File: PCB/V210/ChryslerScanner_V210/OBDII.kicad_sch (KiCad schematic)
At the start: 3 parts

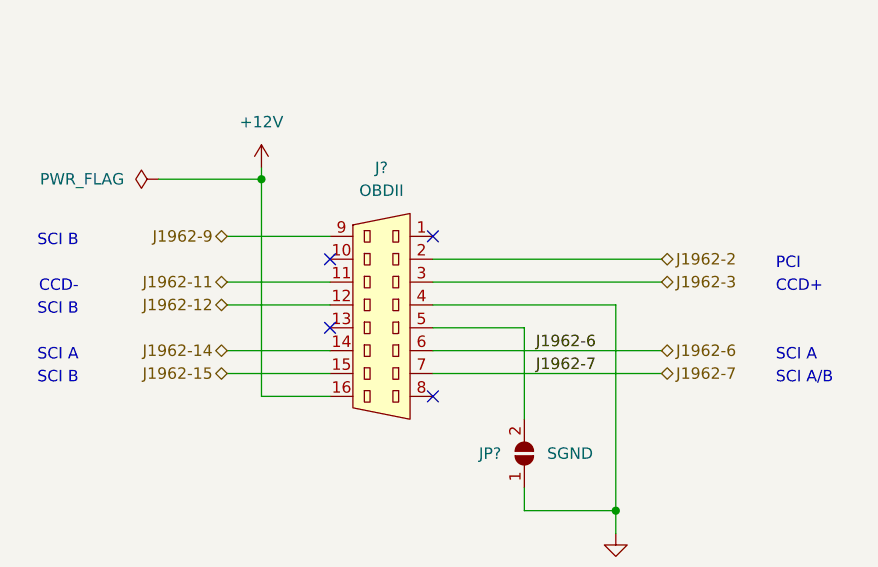
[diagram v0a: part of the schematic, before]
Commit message: Added power supplies. Removed CCD.
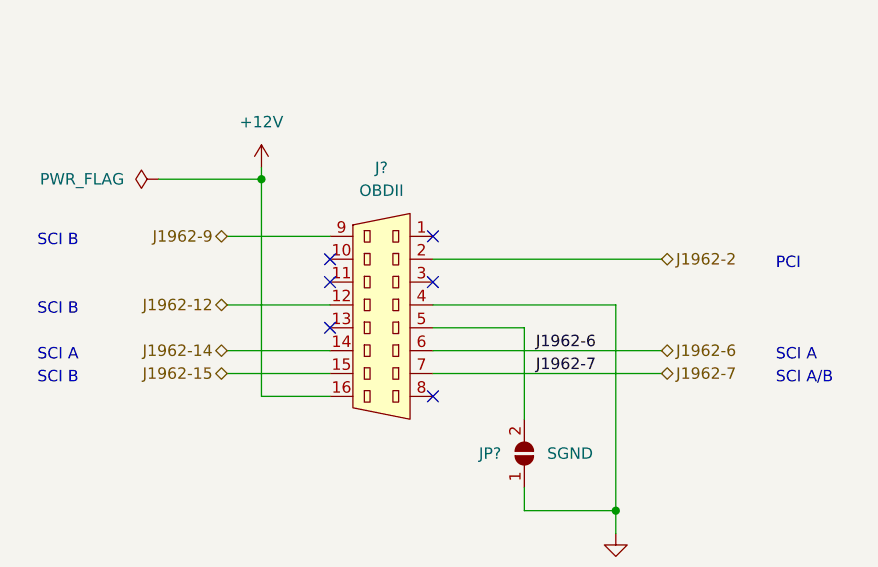
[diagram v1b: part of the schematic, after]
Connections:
- net J1962-11: no longer names the net of J?.11
- net J1962-3: no longer names the net of J?.3
- no-connect marks 4 -> 6
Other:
- note removed: "CCD+"
- note removed: "CCD-"
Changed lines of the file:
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@@
   (title_block
     (title "Chrysler Scanner")
-    (date "2023-06-24")
+    (date "2023-06-25")
     (rev "V2.11")
     (company "andy@britishideas.com")
@@
   (no_connect (at 151.13 92.71))
   (no_connect (at 151.13 110.49))
+  (no_connect (at 151.13 97.79))
+  (no_connect (at 139.7 97.79))
   (wire (pts (xy 151.13 95.25) (xy 176.53 95.25))
     (stroke (width 0) (type default) (color 0 0 0 0))
   )
   (wire (pts (xy 128.27 92.71) (xy 139.7 92.71))
-    (stroke (width 0) (type default) (color 0 0 0 0))
-  )
-  (wire (pts (xy 151.13 97.79) (xy 176.53 97.79))
     (stroke (width 0) (type default) (color 0 0 0 0))
   )
@@
   )
   (wire (pts (xy 128.27 105.41) (xy 139.7 105.41))
-    (stroke (width 0) (type default) (color 0 0 0 0))
-  )
-  (wire (pts (xy 128.27 97.79) (xy 139.7 97.79))
     (stroke (width 0) (type default) (color 0 0 0 0))
   )
@@
     (effects (font (size 1.27 1.27)) (justify left bottom))
   )
-  (text "CCD-" (at 111.76 99.06 180)
-    (effects (font (size 1.27 1.27)) (justify right bottom))
-  )
   (text "PCI" (at 189.23 96.52 0)
     (effects (font (size 1.27 1.27)) (justify left bottom))
@@
   (text "SCI B" (at 111.76 109.22 180)
     (effects (font (size 1.27 1.27)) (justify right bottom))
-  )
-  (text "CCD+" (at 189.23 99.06 0)
-    (effects (font (size 1.27 1.27)) (justify left bottom))
   )
   (text "SCI A" (at 189.23 106.68 0)
@@
     (effects (font (size 1.27 1.27)) (justify left))
   )
-  (hierarchical_label "J1962-3" (shape bidirectional) (at 176.53 97.79 0)
-    (effects (font (size 1.27 1.27)) (justify left))
-  )
-  (hierarchical_label "J1962-11" (shape bidirectional) (at 128.27 97.79 180)
-    (effects (font (size 1.27 1.27)) (justify right))
-  )
   (hierarchical_label "J1962-12" (shape bidirectional) (at 128.27 100.33 180)

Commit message: Completed schematic.
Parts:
- gave numbers to parts that had none: 3
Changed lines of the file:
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@@
   (symbol (lib_id "Connector_Generic:Conn_01x02") (at 135.89 60.96 0) (mirror y) (unit 1)
     (in_bom yes) (on_board yes) (fields_autoplaced)
-    (property "Reference" "J?" (id 0) (at 135.89 54.61 0))
+    (property "Reference" "J3" (id 0) (at 135.89 54.61 0))
     (property "Value" "SCI" (id 1) (at 135.89 57.15 0))
     (property "Footprint" "" (id 2) (at 135.89 60.96 0)
@@
   (symbol (lib_id "Jumper:SolderJumper_2_Open") (at 161.29 116.84 90) (unit 1)
     (in_bom yes) (on_board yes)
-    (property "Reference" "JP?" (id 0) (at 157.48 116.84 90))
+    (property "Reference" "JP1" (id 0) (at 157.48 116.84 90))
     (property "Value" "SGND" (id 1) (at 166.37 116.84 90))
     (property "Footprint" "" (id 2) (at 161.29 116.84 0)
@@
   (symbol (lib_id "power:PWR_FLAG") (at 120.65 86.36 90) (unit 1)
     (in_bom yes) (on_board yes) (fields_autoplaced)
-    (property "Reference" "#FLG?" (id 0) (at 118.745 86.36 0)
+    (property "Reference" "#FLG02" (id 0) (at 118.745 86.36 0)
       (effects (font (size 1.27 1.27)) hide)
     )
@@
   (symbol (lib_id "power:GND") (at 171.45 125.73 0) (unit 1)
     (in_bom yes) (on_board yes) (fields_autoplaced)
-    (property "Reference" "#PWR?" (id 0) (at 171.45 132.08 0)
+    (property "Reference" "#PWR042" (id 0) (at 171.45 132.08 0)
       (effects (font (size 1.27 1.27)) hide)
     )
@@
   (symbol (lib_id "power:+12V") (at 132.08 85.09 0) (unit 1)
     (in_bom yes) (on_board yes) (fields_autoplaced)
-    (property "Reference" "#PWR?" (id 0) (at 132.08 88.9 0)
+    (property "Reference" "#PWR041" (id 0) (at 132.08 88.9 0)
       (effects (font (size 1.27 1.27)) hide)
     )
@@
   (symbol (lib_id "ChryslerScanner:OBDII") (at 143.51 105.41 0) (unit 1)
     (in_bom yes) (on_board yes) (fields_autoplaced)
-    (property "Reference" "J?" (id 0) (at 145.415 85.09 0))
+    (property "Reference" "J4" (id 0) (at 145.415 85.09 0))
     (property "Value" "OBDII" (id 1) (at 145.415 87.63 0))
     (property "Footprint" "" (id 2) (at 143.51 105.41 0)

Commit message: WIP
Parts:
- removed J3: SCI, symbol Connector_Generic:Conn_01x02
- added J2: PCI, Britishideas:PhoenixContact_COMBICON_PT_3, symbol Connector:Screw_Terminal_01x03
- JP1: footprint (none) -> Jumper:SolderJumper-2_P1.3mm_Open_TrianglePad1.0x1.5mm
- renumbered J4 to J3
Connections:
- net +12V: now also J2.1 (Pin_1)
- net GND: now also J2.3 (Pin_3)
- net J1962-2: now also J2.2 (Pin_2)
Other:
- title: Chrysler Scanner -> TJ Diag
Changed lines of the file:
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@@
   (paper "A4")
   (title_block
-    (title "Chrysler Scanner")
-    (date "2023-06-25")
-    (rev "V2.11")
+    (title "TJ Diag")
+    (date "2023-07-01")
+    (rev "V1.00")
     (company "andy@britishideas.com")
     (comment 1 "V210/ChryslerScanner_V210/schematic/ChryslerScanner_V210_schematic.pdf")
@@
     (stroke (width 0) (type default) (color 0 0 0 0))
   )
+  (wire (pts (xy 143.51 59.69) (xy 140.97 59.69))
+    (stroke (width 0) (type default) (color 0 0 0 0))
+  )
   (wire (pts (xy 128.27 92.71) (xy 139.7 92.71))
     (stroke (width 0) (type default) (color 0 0 0 0))
@@
     (stroke (width 0) (type default) (color 0 0 0 0))
   )
-  (wire (pts (xy 140.97 60.96) (xy 149.86 60.96))
+  (wire (pts (xy 140.97 57.15) (xy 149.86 57.15))
     (stroke (width 0) (type default) (color 0 0 0 0))
   )
@@
     (stroke (width 0) (type default) (color 0 0 0 0))
   )
+  (wire (pts (xy 143.51 62.23) (xy 143.51 59.69))
+    (stroke (width 0) (type default) (color 0 0 0 0))
+  )
   (wire (pts (xy 151.13 107.95) (xy 176.53 107.95))
     (stroke (width 0) (type default) (color 0 0 0 0))
   )
-  (wire (pts (xy 140.97 63.5) (xy 149.86 63.5))
+  (wire (pts (xy 143.51 54.61) (xy 140.97 54.61))
     (stroke (width 0) (type default) (color 0 0 0 0))
   )
@@
   )
   (wire (pts (xy 151.13 105.41) (xy 176.53 105.41))
+    (stroke (width 0) (type default) (color 0 0 0 0))
+  )
+  (wire (pts (xy 143.51 52.07) (xy 143.51 54.61))
     (stroke (width 0) (type default) (color 0 0 0 0))
   )
@@
     (effects (font (size 1.27 1.27)) (justify left bottom))
   )
-  (label "J1962-7" (at 162.56 107.95 0)
-    (effects (font (size 1.27 1.27)) (justify left bottom))
-  )
-  (label "J1962-7" (at 149.86 63.5 0)
-    (effects (font (size 1.27 1.27)) (justify left bottom))
-  )
-  (label "J1962-6" (at 149.86 60.96 0)
-    (effects (font (size 1.27 1.27)) (justify left bottom))
-  )
-  (label "J1962-6" (at 162.56 105.41 0)
+  (label "J1962-2" (at 162.56 95.25 0)
+    (effects (font (size 1.27 1.27)) (justify left bottom))
+  )
+  (label "J1962-2" (at 149.86 57.15 0)
     (effects (font (size 1.27 1.27)) (justify left bottom))
   )
@@
     (effects (font (size 1.27 1.27)) (justify right))
   )
-  (symbol (lib_id "Connector_Generic:Conn_01x02") (at 135.89 60.96 0) (mirror y) (unit 1)
-    (in_bom yes) (on_board yes) (fields_autoplaced)
-    (property "Reference" "J3" (id 0) (at 135.89 54.61 0))
-    (property "Value" "SCI" (id 1) (at 135.89 57.15 0))
-    (property "Footprint" "" (id 2) (at 135.89 60.96 0)
-      (effects (font (size 1.27 1.27)) hide)
-    )
-    (property "Datasheet" "~" (id 3) (at 135.89 60.96 0)
+  (symbol (lib_id "Connector:Screw_Terminal_01x03") (at 135.89 57.15 0) (mirror y) (unit 1)
+    (in_bom yes) (on_board yes) (fields_autoplaced)
+    (property "Reference" "J2" (id 0) (at 135.89 48.26 0))
+    (property "Value" "PCI" (id 1) (at 135.89 50.8 0))
+    (property "Footprint" "Britishideas:PhoenixContact_COMBICON_PT_3" (id 2) (at 135.89 57.15 0)
+      (effects (font (size 1.27 1.27)) hide)
+    )
+    (property "Datasheet" "~" (id 3) (at 135.89 57.15 0)
+      (effects (font (size 1.27 1.27)) hide)
+    )
+    (property "manf#" "1935174" (id 4) (at 135.89 57.15 0)
       (effects (font (size 1.27 1.27)) hide)
     )
     (pin "1")
     (pin "2")
+    (pin "3")
   )
   (symbol (lib_id "Jumper:SolderJumper_2_Open") (at 161.29 116.84 90) (unit 1)
@@
     (property "Reference" "JP1" (id 0) (at 157.48 116.84 90))
     (property "Value" "SGND" (id 1) (at 166.37 116.84 90))
-    (property "Footprint" "" (id 2) (at 161.29 116.84 0)
+    (property "Footprint" "Jumper:SolderJumper-2_P1.3mm_Open_TrianglePad1.0x1.5mm" (id 2) (at 161.29 116.84 0)
       (effects (font (size 1.27 1.27)) hide)
     )
@@
   (symbol (lib_id "power:GND") (at 171.45 125.73 0) (unit 1)
     (in_bom yes) (on_board yes) (fields_autoplaced)
-    (property "Reference" "#PWR042" (id 0) (at 171.45 132.08 0)
+    (property "Reference" "#PWR040" (id 0) (at 171.45 132.08 0)
       (effects (font (size 1.27 1.27)) hide)
     )
@@
     (pin "1")
   )
+  (symbol (lib_id "power:GND") (at 143.51 62.23 0) (unit 1)
+    (in_bom yes) (on_board yes) (fields_autoplaced)
+    (property "Reference" "#PWR039" (id 0) (at 143.51 68.58 0)
+      (effects (font (size 1.27 1.27)) hide)
+    )
+    (property "Value" "GND" (id 1) (at 143.51 67.31 0))
+    (property "Footprint" "" (id 2) (at 143.51 62.23 0)
+      (effects (font (size 1.27 1.27)) hide)
+    )
+    (property "Datasheet" "" (id 3) (at 143.51 62.23 0)
+      (effects (font (size 1.27 1.27)) hide)
+    )
+    (pin "1")
+  )
   (symbol (lib_id "power:+12V") (at 132.08 85.09 0) (unit 1)
     (in_bom yes) (on_board yes) (fields_autoplaced)
-    (property "Reference" "#PWR041" (id 0) (at 132.08 88.9 0)
+    (property "Reference" "#PWR037" (id 0) (at 132.08 88.9 0)
       (effects (font (size 1.27 1.27)) hide)
     )
@@
     (pin "1")
   )
+  (symbol (lib_id "power:+12V") (at 143.51 52.07 0) (unit 1)
+    (in_bom yes) (on_board yes) (fields_autoplaced)
+    (property "Reference" "#PWR038" (id 0) (at 143.51 55.88 0)
+      (effects (font (size 1.27 1.27)) hide)
+    )
+    (property "Value" "+12V" (id 1) (at 143.51 46.99 0))
+    (property "Footprint" "" (id 2) (at 143.51 52.07 0)
+      (effects (font (size 1.27 1.27)) hide)
+    )
+    (property "Datasheet" "" (id 3) (at 143.51 52.07 0)
+      (effects (font (size 1.27 1.27)) hide)
+    )
+    (pin "1")
+  )
   (symbol (lib_id "ChryslerScanner:OBDII") (at 143.51 105.41 0) (unit 1)
     (in_bom yes) (on_board yes) (fields_autoplaced)
-    (property "Reference" "J4" (id 0) (at 145.415 85.09 0))
+    (property "Reference" "J3" (id 0) (at 145.415 85.09 0))
     (property "Value" "OBDII" (id 1) (at 145.415 87.63 0))
     (property "Footprint" "" (id 2) (at 143.51 105.41 0)

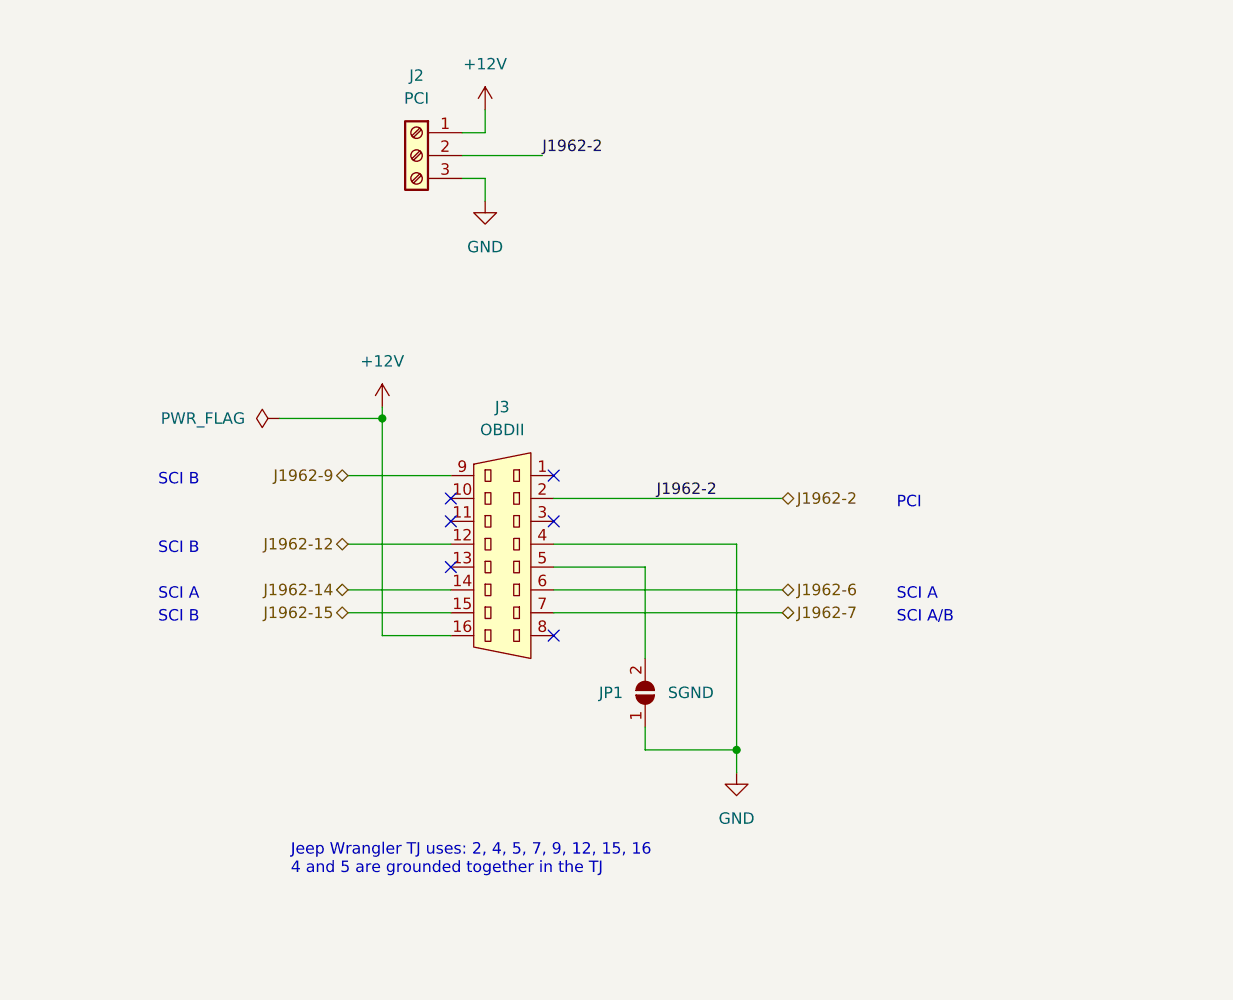
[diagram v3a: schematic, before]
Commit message: Added OBD-II connector.
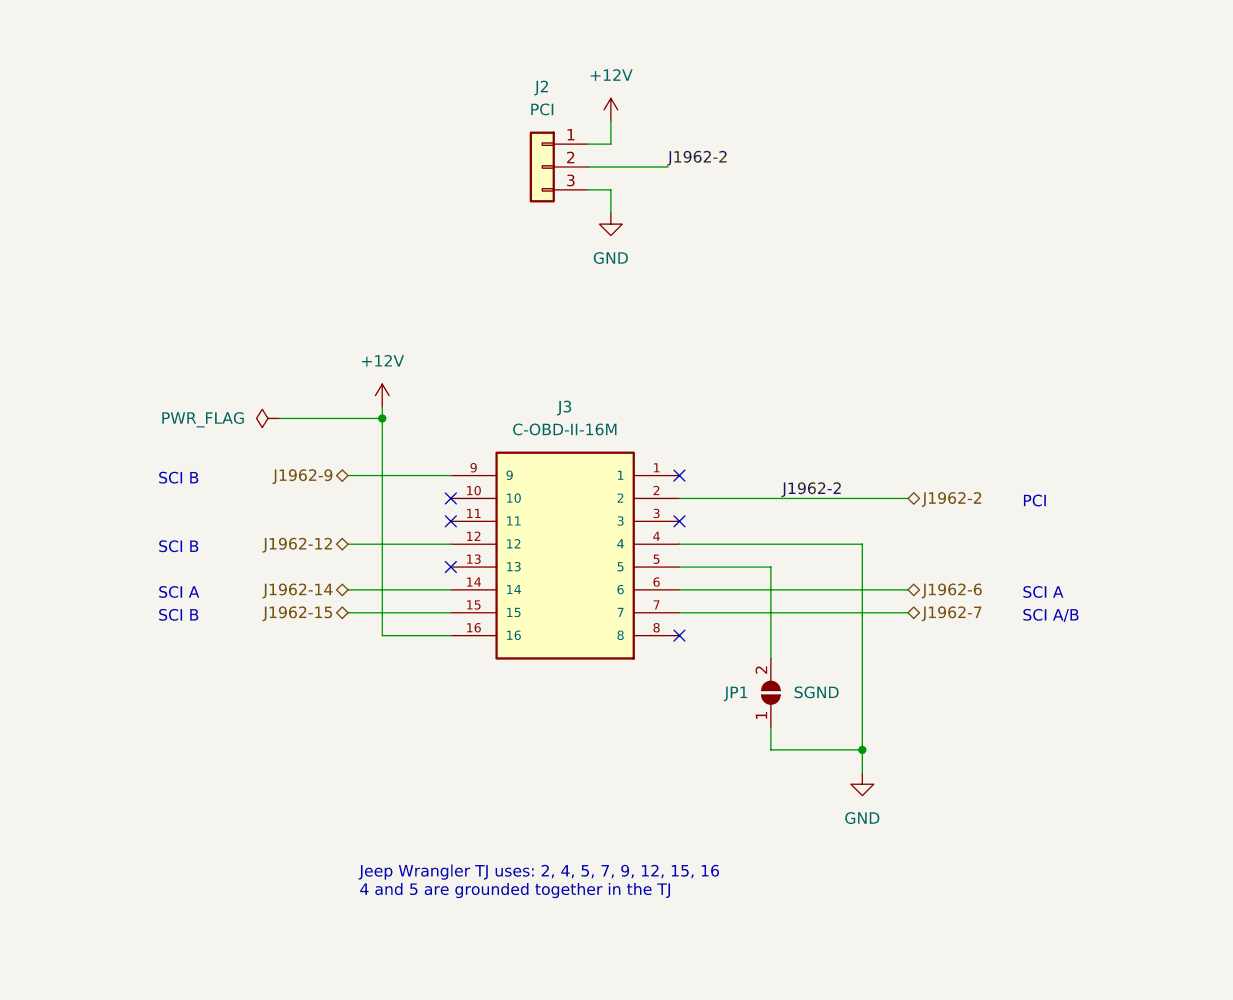
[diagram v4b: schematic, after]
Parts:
- removed J2: PCI, Britishideas:PhoenixContact_COMBICON_PT_3, symbol Connector:Screw_Terminal_01x03
- removed J3: OBDII, symbol ChryslerScanner:OBDII
- added J2: PCI, Connector_PinHeader_2.54mm:PinHeader_1x03_P2.54mm_Vertical, symbol Connector_Generic:Conn_01x03
- added J3: C-OBD-II-16M, ChryslerScanner:COMTECH_C-OBD-II-16M, symbol ChryslerScanner:C-OBD-II-16M
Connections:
- net +12V: now also J2.1 (Pin_1), J3.16
- net GND: now also J2.3 (Pin_3), J3.4
- net J1962-12: now also J3.12
- net J1962-14: now also J3.14
- net J1962-15: now also J3.15
- net J1962-2: now also J2.2 (Pin_2), J3.2
- net J1962-6: now also J3.6
- net J1962-7: now also J3.7
- net J1962-9: now also J3.9
- net at JP1.2 (B): now also J3.5
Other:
- moved on the sheet: JP1

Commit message: Added CCD back in - needed for early TJs.
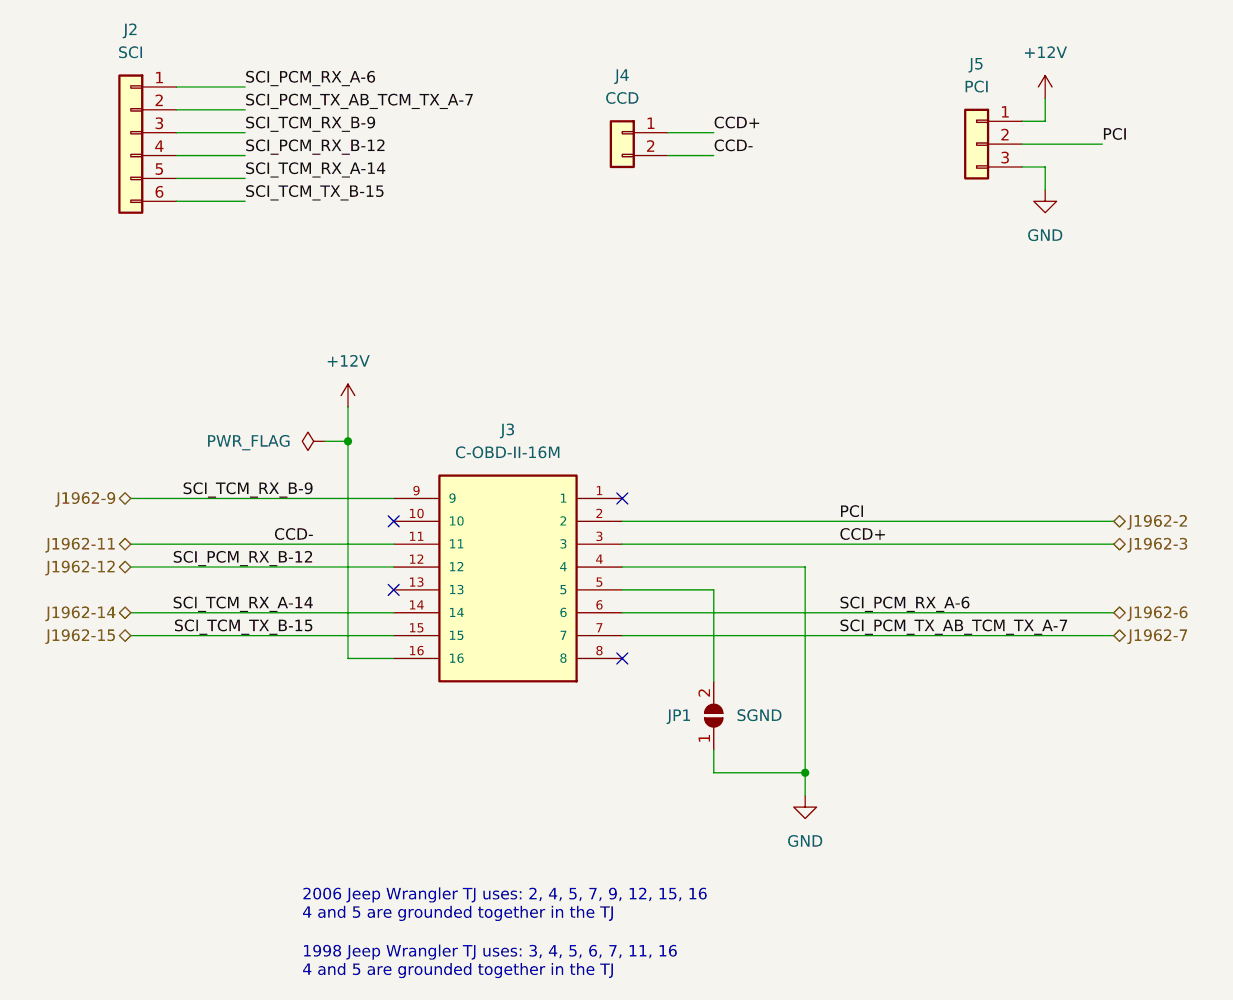
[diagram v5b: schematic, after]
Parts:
- added J2: SCI, Connector_JST:JST_PH_B6B-PH-K_1x06_P2.00mm_Vertical, symbol Connector_Generic:Conn_01x06
- added J4: CCD, Connector_JST:JST_PH_B2B-PH-K_1x02_P2.00mm_Vertical, symbol Connector_Generic:Conn_01x02
- J5: renamed from J2; footprint Connector_PinHeader_2.54mm:PinHeader_1x03_P2.54mm_Vertical -> Connector_JST:JST_PH_B3B-PH-K_1x03_P2.00mm_Vertical; manf# (none) -> B3B-PH-KL
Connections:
- net J1962-12: now also J2.4 (Pin_4)
- net J1962-14: now also J2.5 (Pin_5)
- net J1962-15: now also J2.6 (Pin_6)
- net J1962-6: now also J2.1 (Pin_1)
- net J1962-7: now also J2.2 (Pin_2)
- net J1962-9: now also J2.3 (Pin_3)
- net J1962-11: now reaches J3.11
- net J1962-11: now also J4.2 (Pin_2)
- net J1962-3: now reaches J3.3
- net J1962-3: now also J4.1 (Pin_1)
- no-connect marks 6 -> 4
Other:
- note added: "1998 Jeep Wrangler TJ uses: 3, 4, 5, 6, 7, 11, 16 4 and 5 are grounded together in the TJ"
- note added: "2006 Jeep Wrangler TJ uses: 2, 4, 5, 7, 9, 12, 15, 16 4 and 5 are grounded together in the TJ"
- note removed: "Jeep Wrangler TJ uses: 2, 4, 5, 7, 9, 12, 15, 16 4 and 5 are grounded together in the TJ"
- note removed: "PCI"
- note removed: "SCI A"
- note removed: "SCI A/B"
- note removed: "SCI B"
- moved on the sheet: J3, J5, JP1
